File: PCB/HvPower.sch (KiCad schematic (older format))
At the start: 40 parts

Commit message: Add missing footprints
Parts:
- NT? (x2): footprint (none) -> Parts:NetTie-2
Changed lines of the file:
@@
 F 0 "NT?" H 3900 3631 50  0000 C CNN
 F 1 "Net-Tie_2" H 3900 3540 50  0000 C CNN
-F 2 "" H 3900 3450 50  0001 C CNN
+F 2 "Parts:NetTie-2" H 3900 3450 50  0001 C CNN
 F 3 "~" H 3900 3450 50  0001 C CNN
 	1    3900 3450
@@
 F 0 "NT?" H 3900 6281 50  0000 C CNN
 F 1 "Net-Tie_2" H 3900 6190 50  0000 C CNN
-F 2 "" H 3900 6100 50  0001 C CNN
+F 2 "Parts:NetTie-2" H 3900 6100 50  0001 C CNN
 F 3 "~" H 3900 6100 50  0001 C CNN
 	1    3900 6100

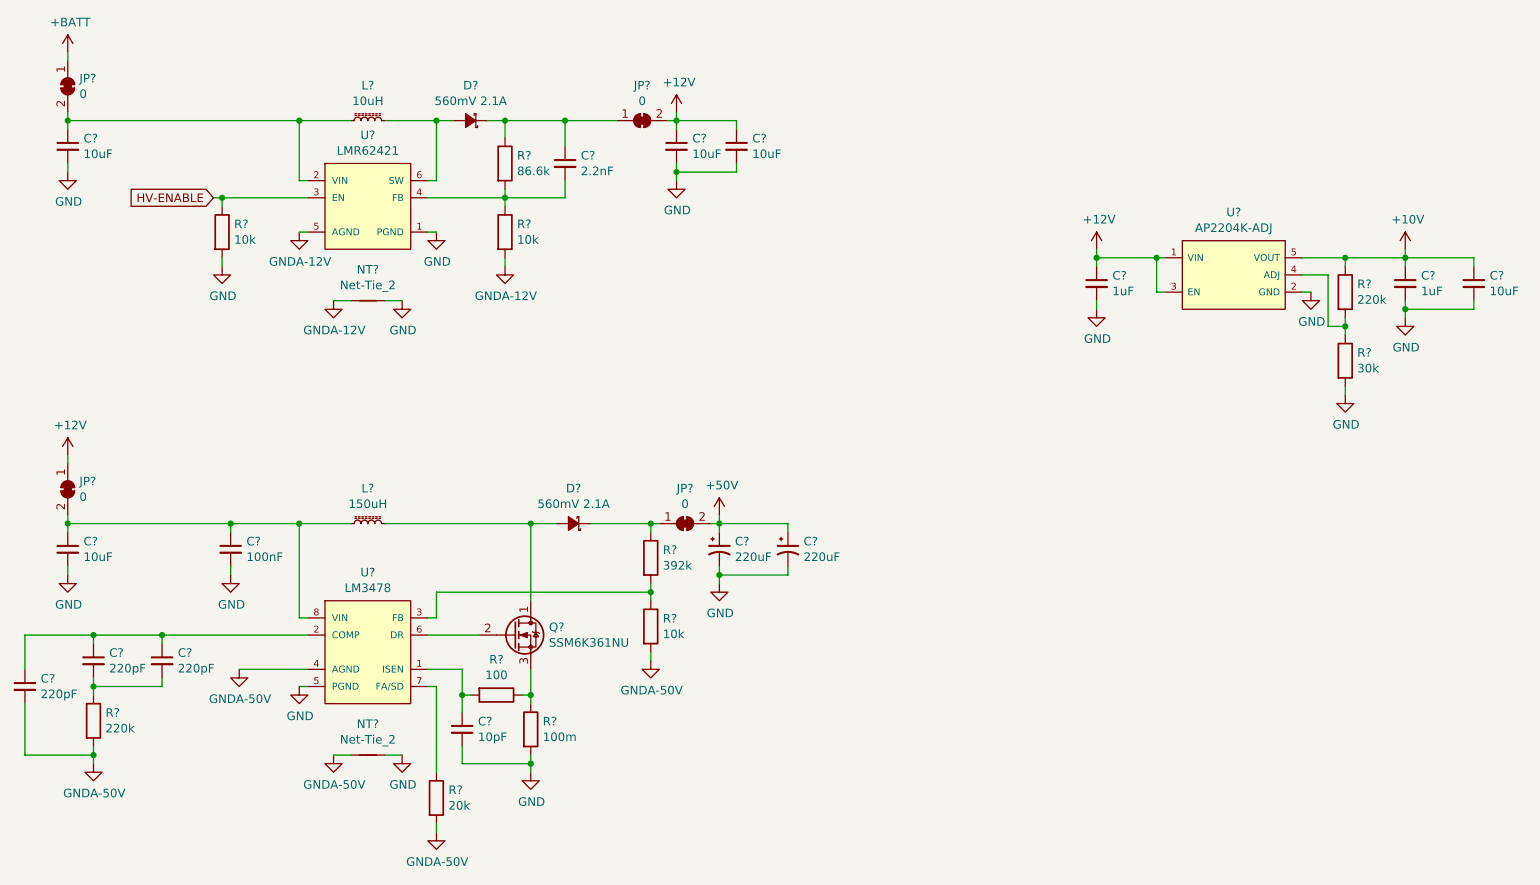
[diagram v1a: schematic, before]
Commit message: Annotate schematic, simplify transmit circuit, shuffle receive opamp stages, reorder buttons so they match net names, reorder connectors to simplify routing, begin arranging parts on PCB
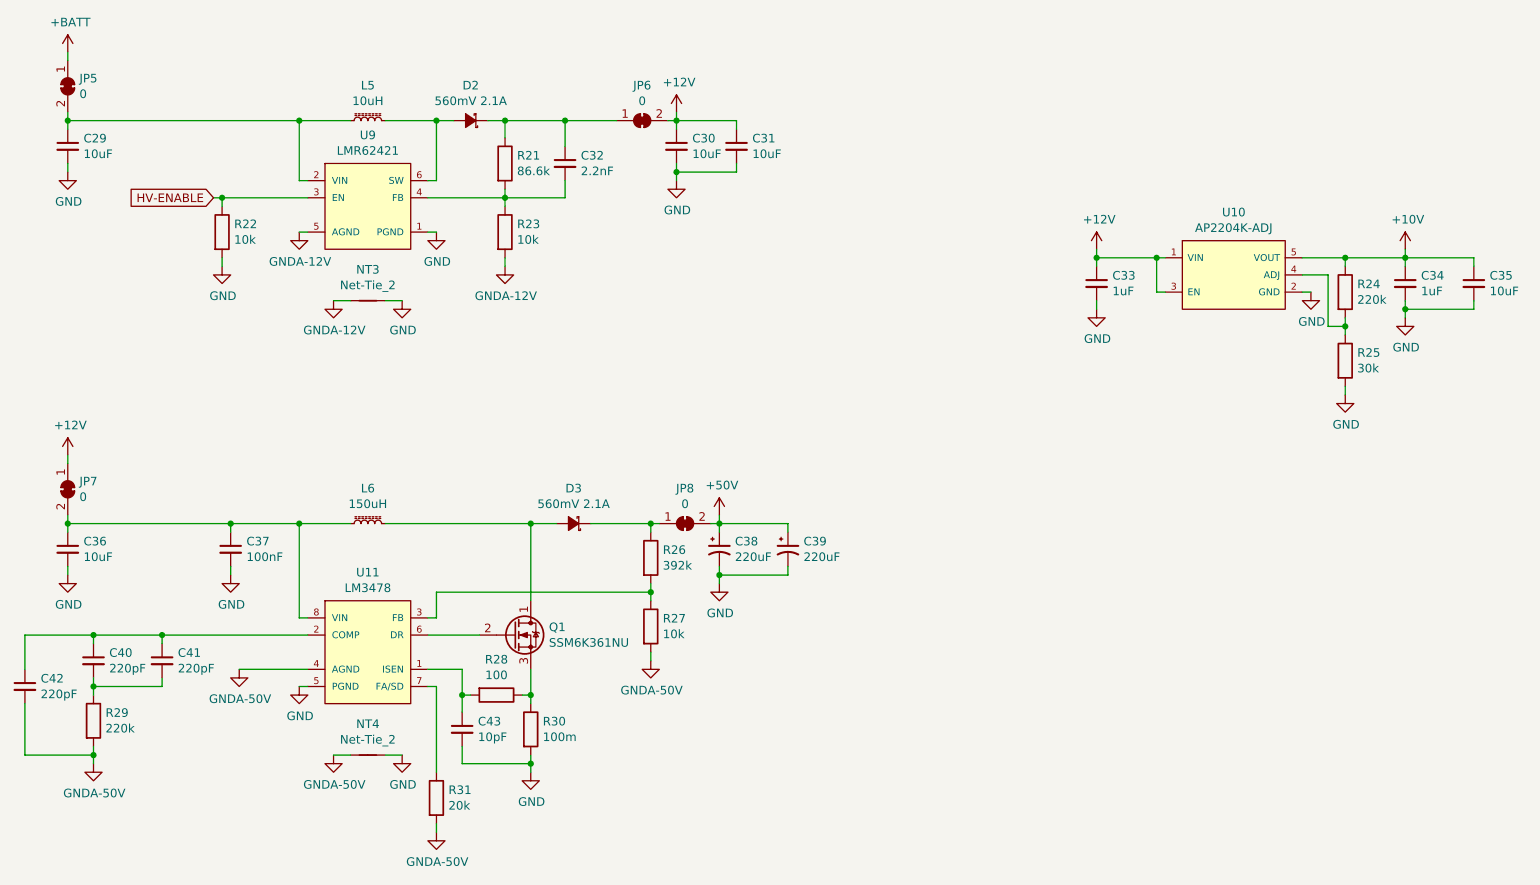
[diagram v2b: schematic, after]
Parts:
- gave numbers to parts that had none: 40

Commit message: Remove unnecessary series resistors, rearrange connections on FPGA and microcontroller, rearrange debug pins, layout most of FPGA and microcontroller sections
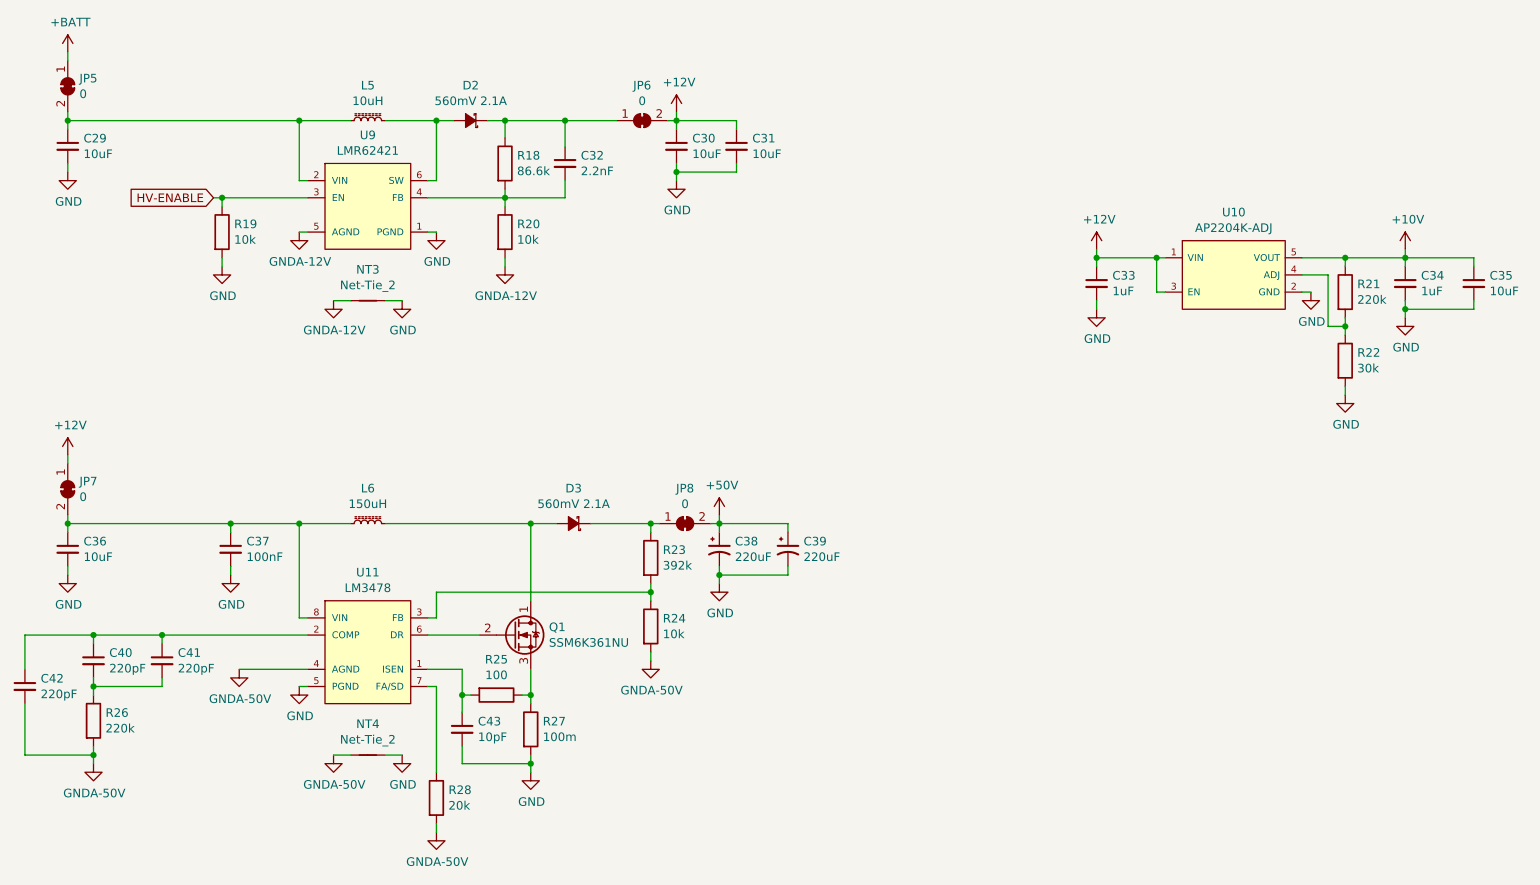
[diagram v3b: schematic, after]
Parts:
- renumbered R21 to R18, R22 to R19, R23 to R20, R24 to R21, R25 to R22, R26 to R23, R27 to R24, R28 to R25, R29 to R26, R30 to R27, R31 to R28
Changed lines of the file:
@@
 Connection ~ 5700 2400
 $Comp
-L Device:R R21
+L Device:R R18
 U 1 1 5DE0A120
 P 4700 2650
-F 0 "R21" H 4770 2696 50  0000 L CNN
+F 0 "R18" H 4770 2696 50  0000 L CNN
 F 1 "86.6k" H 4770 2605 50  0000 L CNN
 F 2 "Capacitors_SMD:C_0603_HandSoldering" V 4630 2650 50  0001 C CNN
@@
 $EndComp
 $Comp
-L Device:R R23
+L Device:R R20
 U 1 1 5DE0BC20
 P 4700 3050
-F 0 "R23" H 4770 3096 50  0000 L CNN
+F 0 "R20" H 4770 3096 50  0000 L CNN
 F 1 "10k" H 4770 3005 50  0000 L CNN
 F 2 "Capacitors_SMD:C_0603_HandSoldering" V 4630 3050 50  0001 C CNN
@@
 	3000 2850 3050 2850
 $Comp
-L Device:R R22
+L Device:R R19
 U 1 1 5DE108CD
 P 3050 3050
-F 0 "R22" H 3120 3096 50  0000 L CNN
+F 0 "R19" H 3120 3096 50  0000 L CNN
 F 1 "10k" H 3120 3005 50  0000 L CNN
 F 2 "Capacitors_SMD:C_0603_HandSoldering" V 2980 3050 50  0001 C CNN
@@
 $EndComp
 $Comp
-L Device:R R27
+L Device:R R24
 U 1 1 5DE5F8A5
 P 5550 5350
-F 0 "R27" H 5620 5396 50  0000 L CNN
+F 0 "R24" H 5620 5396 50  0000 L CNN
 F 1 "10k" H 5620 5305 50  0000 L CNN
 F 2 "Capacitors_SMD:C_0603_HandSoldering" V 5480 5350 50  0001 C CNN
@@
 	5550 5200 5550 5150
 $Comp
-L Device:R R26
+L Device:R R23
 U 1 1 5DE602EE
 P 5550 4950
-F 0 "R26" H 5620 4996 50  0000 L CNN
+F 0 "R23" H 5620 4996 50  0000 L CNN
 F 1 "392k" H 5620 4905 50  0000 L CNN
 F 2 "Capacitors_SMD:C_0603_HandSoldering" V 5480 4950 50  0001 C CNN
@@
 	3700 6100 3800 6100
 $Comp
-L Device:R R30
+L Device:R R27
 U 1 1 5DE83FB9
 P 4850 5950
-F 0 "R30" H 4920 5996 50  0000 L CNN
+F 0 "R27" H 4920 5996 50  0000 L CNN
 F 1 "100m" H 4920 5905 50  0000 L CNN
 F 2 "Capacitors_SMD:C_0603_HandSoldering" V 4780 5950 50  0001 C CNN
@@
 	4850 5600 4850 5750
 $Comp
-L Device:R R28
+L Device:R R25
 U 1 1 5DE8B420
 P 4650 5750
-F 0 "R28" V 4443 5750 50  0000 C CNN
+F 0 "R25" V 4443 5750 50  0000 C CNN
 F 1 "100" V 4534 5750 50  0000 C CNN
 F 2 "Capacitors_SMD:C_0603_HandSoldering" V 4580 5750 50  0001 C CNN
@@
 	3150 5600 3550 5600
 $Comp
-L Device:R R31
+L Device:R R28
 U 1 1 5DEAF609
 P 4300 6350
-F 0 "R31" H 4370 6396 50  0000 L CNN
+F 0 "R28" H 4370 6396 50  0000 L CNN
 F 1 "20k" H 4370 6305 50  0000 L CNN
 F 2 "Capacitors_SMD:C_0603_HandSoldering" V 4230 6350 50  0001 C CNN
@@
 	2700 5400 2700 5450
 $Comp
-L Device:R R29
+L Device:R R26
 U 1 1 5DEED067
 P 2300 5900
-F 0 "R29" H 2370 5946 50  0000 L CNN
+F 0 "R26" H 2370 5946 50  0000 L CNN
 F 1 "220k" H 2370 5855 50  0000 L CNN
 F 2 "Capacitors_SMD:C_0603_HandSoldering" V 2230 5900 50  0001 C CNN
@@
 	9350 3200 9600 3200
 $Comp
-L Device:R R24
+L Device:R R21
 U 1 1 5E0E52C3
 P 9600 3400
-F 0 "R24" H 9670 3446 50  0000 L CNN
+F 0 "R21" H 9670 3446 50  0000 L CNN
 F 1 "220k" H 9670 3355 50  0000 L CNN
 F 2 "Capacitors_SMD:C_0603_HandSoldering" V 9530 3400 50  0001 C CNN
@@
 $EndComp
 $Comp
-L Device:R R25
+L Device:R R22
 U 1 1 5E0E587B
 P 9600 3800
-F 0 "R25" H 9670 3846 50  0000 L CNN
+F 0 "R22" H 9670 3846 50  0000 L CNN
 F 1 "30k" H 9670 3755 50  0000 L CNN
 F 2 "Capacitors_SMD:C_0603_HandSoldering" V 9530 3800 50  0001 C CNN

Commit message: Fix resistors to use resistor footprints
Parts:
- R18, R19, R20, R21, R22, R23, R24, R25, R26, R27, R28: footprint Capacitors_SMD:C_0603_HandSoldering -> Resistors_SMD:R_0603_HandSoldering
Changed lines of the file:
@@
 F 0 "R18" H 4770 2696 50  0000 L CNN
 F 1 "86.6k" H 4770 2605 50  0000 L CNN
-F 2 "Capacitors_SMD:C_0603_HandSoldering" V 4630 2650 50  0001 C CNN
+F 2 "Resistors_SMD:R_0603_HandSoldering" V 4630 2650 50  0001 C CNN
 F 3 "https://www.digikey.ca/product-detail/en/stackpole-electronics-inc/RMCF0603FT86K6/RMCF0603FT86K6CT-ND/1943115" H 4700 2650 50  0001 C CNN
 	1    4700 2650
@@
 F 0 "R20" H 4770 3096 50  0000 L CNN
 F 1 "10k" H 4770 3005 50  0000 L CNN
-F 2 "Capacitors_SMD:C_0603_HandSoldering" V 4630 3050 50  0001 C CNN
+F 2 "Resistors_SMD:R_0603_HandSoldering" V 4630 3050 50  0001 C CNN
 F 3 "https://www.digikey.ca/product-detail/en/stackpole-electronics-inc/RMCF0603FT10K0/RMCF0603FT10K0CT-ND/1943057" H 4700 3050 50  0001 C CNN
 	1    4700 3050
@@
 F 0 "R19" H 3120 3096 50  0000 L CNN
 F 1 "10k" H 3120 3005 50  0000 L CNN
-F 2 "Capacitors_SMD:C_0603_HandSoldering" V 2980 3050 50  0001 C CNN
+F 2 "Resistors_SMD:R_0603_HandSoldering" V 2980 3050 50  0001 C CNN
 F 3 "https://www.digikey.ca/product-detail/en/stackpole-electronics-inc/RMCF0603FT10K0/RMCF0603FT10K0CT-ND/1943057" H 3050 3050 50  0001 C CNN
 	1    3050 3050
@@
 F 0 "R24" H 5620 5396 50  0000 L CNN
 F 1 "10k" H 5620 5305 50  0000 L CNN
-F 2 "Capacitors_SMD:C_0603_HandSoldering" V 5480 5350 50  0001 C CNN
+F 2 "Resistors_SMD:R_0603_HandSoldering" V 5480 5350 50  0001 C CNN
 F 3 "https://www.digikey.ca/product-detail/en/stackpole-electronics-inc/RMCF0603FT10K0/RMCF0603FT10K0CT-ND/1943057" H 5550 5350 50  0001 C CNN
 	1    5550 5350
@@
 F 0 "R23" H 5620 4996 50  0000 L CNN
 F 1 "392k" H 5620 4905 50  0000 L CNN
-F 2 "Capacitors_SMD:C_0603_HandSoldering" V 5480 4950 50  0001 C CNN
+F 2 "Resistors_SMD:R_0603_HandSoldering" V 5480 4950 50  0001 C CNN
 F 3 "https://www.digikey.ca/product-detail/en/stackpole-electronics-inc/RMCF0603FT392K/RMCF0603FT392KCT-ND/1943135" H 5550 4950 50  0001 C CNN
 	1    5550 4950
@@
 F 0 "R27" H 4920 5996 50  0000 L CNN
 F 1 "100m" H 4920 5905 50  0000 L CNN
-F 2 "Capacitors_SMD:C_0603_HandSoldering" V 4780 5950 50  0001 C CNN
+F 2 "Resistors_SMD:R_0603_HandSoldering" V 4780 5950 50  0001 C CNN
 F 3 "https://www.digikey.ca/product-detail/en/panasonic-electronic-components/ERJ-3RSFR10V/P.10AJCT-ND/308098" H 4850 5950 50  0001 C CNN
 	1    4850 5950
@@
 F 0 "R25" V 4443 5750 50  0000 C CNN
 F 1 "100" V 4534 5750 50  0000 C CNN
-F 2 "Capacitors_SMD:C_0603_HandSoldering" V 4580 5750 50  0001 C CNN
+F 2 "Resistors_SMD:R_0603_HandSoldering" V 4580 5750 50  0001 C CNN
 F 3 "https://www.digikey.ca/product-detail/en/stackpole-electronics-inc/RMCF0603FT100R/RMCF0603FT100RCT-ND/1942965" H 4650 5750 50  0001 C CNN
 	1    4650 5750
@@
 F 0 "R28" H 4370 6396 50  0000 L CNN
 F 1 "20k" H 4370 6305 50  0000 L CNN
-F 2 "Capacitors_SMD:C_0603_HandSoldering" V 4230 6350 50  0001 C CNN
+F 2 "Resistors_SMD:R_0603_HandSoldering" V 4230 6350 50  0001 C CNN
 F 3 "https://www.digikey.ca/product-detail/en/stackpole-electronics-inc/RMCF0603FT20K0/RMCF0603FT20K0CT-ND/1943075" H 4300 6350 50  0001 C CNN
 	1    4300 6350
@@
 F 0 "R26" H 2370 5946 50  0000 L CNN
 F 1 "220k" H 2370 5855 50  0000 L CNN
-F 2 "Capacitors_SMD:C_0603_HandSoldering" V 2230 5900 50  0001 C CNN
+F 2 "Resistors_SMD:R_0603_HandSoldering" V 2230 5900 50  0001 C CNN
 F 3 "https://www.digikey.ca/product-detail/en/stackpole-electronics-inc/RMCF0603FT220K/RMCF0603FT220KCT-ND/2417988" H 2300 5900 50  0001 C CNN
 	1    2300 5900
@@
 F 0 "R21" H 9670 3446 50  0000 L CNN
 F 1 "220k" H 9670 3355 50  0000 L CNN
-F 2 "Capacitors_SMD:C_0603_HandSoldering" V 9530 3400 50  0001 C CNN
+F 2 "Resistors_SMD:R_0603_HandSoldering" V 9530 3400 50  0001 C CNN
 F 3 "https://www.digikey.ca/product-detail/en/stackpole-electronics-inc/RMCF0603FT220K/RMCF0603FT220KCT-ND/2417988" H 9600 3400 50  0001 C CNN
 	1    9600 3400
@@
 F 0 "R22" H 9670 3846 50  0000 L CNN
 F 1 "30k" H 9670 3755 50  0000 L CNN
-F 2 "Capacitors_SMD:C_0603_HandSoldering" V 9530 3800 50  0001 C CNN
+F 2 "Resistors_SMD:R_0603_HandSoldering" V 9530 3800 50  0001 C CNN
 F 3 "https://www.digikey.ca/product-detail/en/stackpole-electronics-inc/RMCF0603FT30K0/RMCF0603FT30K0CT-ND/1943086" H 9600 3800 50  0001 C CNN
 	1    9600 3800

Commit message: Fix incorrect footprint on power supply diodes
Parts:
- D2, D3: footprint Diodes_SMD:D_SOD-123F -> Parts:DO-220AA
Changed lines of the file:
@@
 F 0 "D3" H 5100 4545 50  0000 C CNN
 F 1 "560mV 2.1A" H 5100 4636 50  0000 C CNN
-F 2 "Diodes_SMD:D_SOD-123F" V 5100 4750 50  0001 C CNN
+F 2 "Parts:DO-220AA" V 5100 4750 50  0001 C CNN
 F 3 "https://www.digikey.ca/product-detail/en/vishay-semiconductor-diodes-division/V3PM10-M3-H/112-V3PM10-M3-HCT-ND/10638970" V 5100 4750 50  0001 C CNN
 	1    5100 4750
@@
 F 0 "D2" H 4500 2195 50  0000 C CNN
 F 1 "560mV 2.1A" H 4500 2286 50  0000 C CNN
-F 2 "Diodes_SMD:D_SOD-123F" V 4500 2400 50  0001 C CNN
+F 2 "Parts:DO-220AA" V 4500 2400 50  0001 C CNN
 F 3 "https://www.digikey.ca/product-detail/en/vishay-semiconductor-diodes-division/V3PM10-M3-H/112-V3PM10-M3-HCT-ND/10638970" V 4500 2400 50  0001 C CNN
 	1    4500 2400
